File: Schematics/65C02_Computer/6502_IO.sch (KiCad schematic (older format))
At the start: 22 parts

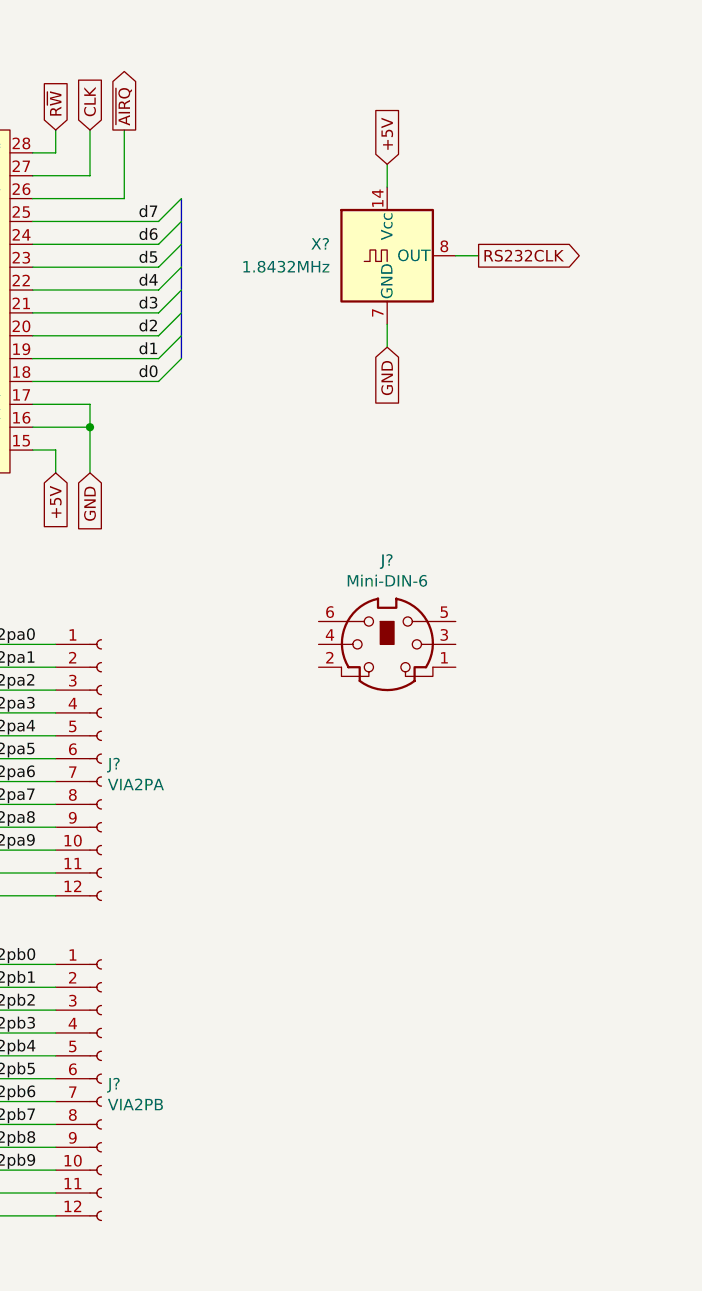
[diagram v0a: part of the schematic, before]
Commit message: Added keyboard microcontroller
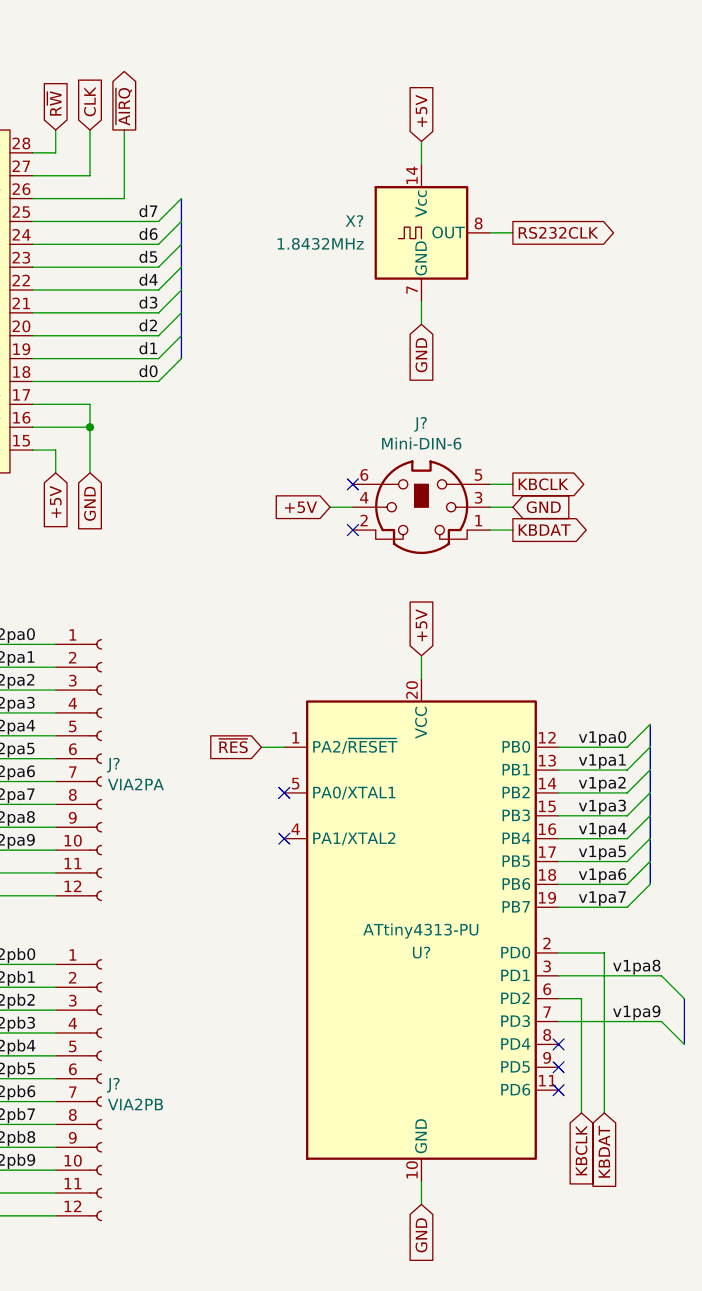
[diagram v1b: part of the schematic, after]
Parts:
- added U?: ATtiny4313-PU, Package_DIP:DIP-20_W7.62mm, symbol MCU_Microchip_ATtiny:ATtiny4313-PU
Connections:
- net +5V: now also J?.4, U?.20 (VCC)
- net GND: now also J?.3, U?.10 (GND)
- net v1pa0: now also U?.12 (PB0)
- net v1pa1: now also U?.13 (PB1)
- net v1pa2: now also U?.14 (PB2)
- net v1pa3: now also U?.15 (PB3)
- net v1pa4: now also U?.16 (PB4)
- net v1pa5: now also U?.17 (PB5)
- net v1pa6: now also U?.18 (PB6)
- net v1pa7: now also U?.19 (PB7)
- net v1pa8: now also U?.3 (PD1)
- net v1pa9: now also U?.7 (PD3)
- net ~RES: now also U?.1 (PA2/~RESET)
- net KBDAT: now reaches J?.1
- net KBDAT: now also U?.2 (PD0)
- net KBCLK: now reaches J?.5
- net KBCLK: now also U?.6 (PD2)
- no-connect marks 9 -> 16
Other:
- moved on the sheet: J?, X?
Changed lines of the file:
@@
 Wire Wire Line
 	5700 750  5700 1050
-Text GLabel 9400 1150 1    50   Input ~ 0
+Text GLabel 9550 1050 1    50   Input ~ 0
 +5V
-Text GLabel 9400 1950 3    50   Input ~ 0
+Text GLabel 9550 1850 3    50   Input ~ 0
 GND
 Wire Wire Line
-	9400 1950 9400 1850
-Wire Wire Line
-	9400 1150 9400 1250
-Text GLabel 9800 1550 2    50   Output ~ 0
+	9550 1850 9550 1750
+Wire Wire Line
+	9550 1050 9550 1150
+Text GLabel 9950 1450 2    50   Output ~ 0
 RS232CLK
 Wire Wire Line
-	9700 1550 9800 1550
+	9850 1450 9950 1450
 Wire Wire Line
 	2350 1950 2500 1950
@@
 L Connector:Mini-DIN-6 J?
 U 1 1 5F701D58
-P 9400 3250
-F 0 "J?" H 9400 3617 50  0000 C CNN
-F 1 "Mini-DIN-6" H 9400 3526 50  0000 C CNN
-F 2 "65C02_Computer:mini_din-6" H 9400 3250 50  0001 C CNN
-F 3 "http://service.powerdynamics.com/ec/Catalog17/Section%2011.pdf" H 9400 3250 50  0001 C CNN
-	1    9400 3250
+P 9550 2650
+F 0 "J?" H 9550 3017 50  0000 C CNN
+F 1 "Mini-DIN-6" H 9550 2926 50  0000 C CNN
+F 2 "65C02_Computer:mini_din-6" H 9550 2650 50  0001 C CNN
+F 3 "http://service.powerdynamics.com/ec/Catalog17/Section%2011.pdf" H 9550 2650 50  0001 C CNN
+	1    9550 2650
 	1    0    0    -1
 $EndComp
@@
 L Oscillator:ACO-xxxMHz X?
 U 1 1 5F4F8D3E
-P 9400 1550
+P 9550 1450
 AR Path="/5F4F8D3E" Ref="X?"  Part="1"
 AR Path="/5F14295C/5F4F8D3E" Ref="X?"  Part="1"
-F 0 "X?" H 9150 1600 50  0000 R CNN
-F 1 "1.8432MHz" H 9150 1500 50  0000 R CNN
-F 2 "Oscillator:Oscillator_DIP-14" H 9850 1200 50  0001 C CNN
-F 3 "http://www.conwin.com/datasheets/cx/cx030.pdf" H 9300 1550 50  0001 C CNN
-	1    9400 1550
+F 0 "X?" H 9300 1500 50  0000 R CNN
+F 1 "1.8432MHz" H 9300 1400 50  0000 R CNN
+F 2 "Oscillator:Oscillator_DIP-14" H 10000 1100 50  0001 C CNN
+F 3 "http://www.conwin.com/datasheets/cx/cx030.pdf" H 9450 1450 50  0001 C CNN
+	1    9550 1450
 	1    0    0    -1
 $EndComp
@@
 Entry Wire Line
 	7550 5450 7650 5550
+Text GLabel 9950 2550 2    50   Output ~ 0
+KBCLK
+Text GLabel 9950 2750 2    50   Output ~ 0
+KBDAT
+Text GLabel 9950 2650 2    50   Input ~ 0
+GND
+Text GLabel 9150 2650 0    50   Input ~ 0
++5V
+Wire Wire Line
+	9150 2650 9250 2650
+Wire Wire Line
+	9850 2650 9950 2650
+Wire Wire Line
+	9850 2550 9950 2550
+Wire Wire Line
+	9850 2750 9950 2750
+NoConn ~ 9250 2550
+NoConn ~ 9250 2750
+Text GLabel 9550 3300 1    50   Input ~ 0
++5V
+Text GLabel 9550 5700 3    50   Input ~ 0
+GND
+Text GLabel 8850 3700 0    50   Input ~ 0
+~RES
+Text Label 10450 3700 2    50   ~ 0
+v1pa0
+Text Label 10450 3800 2    50   ~ 0
+v1pa1
+Text Label 10450 3900 2    50   ~ 0
+v1pa2
+Text Label 10450 4000 2    50   ~ 0
+v1pa3
+Text Label 10450 4100 2    50   ~ 0
+v1pa4
+Text Label 10450 4200 2    50   ~ 0
+v1pa5
+Text Label 10450 4300 2    50   ~ 0
+v1pa6
+Text Label 10450 4400 2    50   ~ 0
+v1pa7
+Entry Wire Line
+	10450 3700 10550 3600
+Entry Wire Line
+	10450 3800 10550 3700
+Entry Wire Line
+	10450 3900 10550 3800
+Entry Wire Line
+	10450 4000 10550 3900
+Entry Wire Line
+	10450 4100 10550 4000
+Entry Wire Line
+	10450 4200 10550 4100
+Entry Wire Line
+	10450 4300 10550 4200
+Entry Wire Line
+	10450 4400 10550 4300
+Wire Wire Line
+	10150 3700 10450 3700
+Wire Wire Line
+	10150 3800 10450 3800
+Wire Wire Line
+	10150 3900 10450 3900
+Wire Wire Line
+	10150 4000 10450 4000
+Wire Wire Line
+	10150 4100 10450 4100
+Wire Wire Line
+	10150 4200 10450 4200
+Wire Wire Line
+	10150 4300 10450 4300
+Wire Wire Line
+	10150 4400 10450 4400
+Text GLabel 10350 5300 3    50   Input ~ 0
+KBDAT
+$Comp
+L MCU_Microchip_ATtiny:ATtiny4313-PU U?
+U 1 1 5E5D2E2B
+P 9550 4500
+F 0 "U?" H 9550 4400 50  0000 C CNN
+F 1 "ATtiny4313-PU" H 9550 4500 50  0000 C CNN
+F 2 "Package_DIP:DIP-20_W7.62mm" H 9550 4500 50  0001 C CIN
+F 3 "http://ww1.microchip.com/downloads/en/DeviceDoc/doc8246.pdf" H 9550 4500 50  0001 C CNN
+	1    9550 4500
+	1    0    0    -1
+$EndComp
+Wire Wire Line
+	8850 3700 8950 3700
+Wire Wire Line
+	10150 4800 10250 4800
+Text GLabel 10250 5300 3    50   Input ~ 0
+KBCLK
+NoConn ~ 8950 3900
+NoConn ~ 8950 4100
+Text Label 10600 4700 2    50   ~ 0
+v1pa8
+Text Label 10600 4900 2    50   ~ 0
+v1pa9
+Wire Wire Line
+	10250 5300 10250 4800
+Wire Wire Line
+	10350 5300 10350 4600
+Wire Wire Line
+	10150 4600 10350 4600
+Wire Wire Line
+	10150 4700 10600 4700
+Wire Wire Line
+	10150 4900 10600 4900
+Wire Wire Line
+	9550 5700 9550 5600
+Wire Wire Line
+	9550 3300 9550 3400
+Entry Wire Line
+	10600 4700 10700 4800
+Entry Wire Line
+	10600 4900 10700 5000
+Wire Bus Line
+	10700 5000 10700 4800
+NoConn ~ 10150 5000
+NoConn ~ 10150 5100
+NoConn ~ 10150 5200
 Wire Bus Line
 	5500 3000 5500 3400
@@
 	5950 3850 5950 4650
 Wire Bus Line
+	10550 3600 10550 4300
+Wire Bus Line
+	7550 4550 7550 5450
+Wire Bus Line
+	7550 3150 7550 4050
+Wire Bus Line
 	3450 4400 3450 5300
 Wire Bus Line
@@
 Wire Bus Line
 	1050 3000 1050 4100
-Wire Bus Line
-	7550 3150 7550 4050
-Wire Bus Line
-	7550 4550 7550 5450
 $EndSCHEMATC

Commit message: Various updates to schematic
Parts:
- added D4: BLINK, LED_THT:LED_D5.0mm_Clear, symbol Device:LED
- added R12: 270, Resistor_THT:R_Axial_DIN0207_L6.3mm_D2.5mm_P7.62mm_Horizontal, symbol Device:R
- C14, C15, C16: renamed from C?; footprint (none) -> Capacitor_THT:C_Disc_D3.4mm_W2.1mm_P2.50mm
- D1, D2, D3: renamed from D?; footprint (none) -> LED_THT:LED_D5.0mm_Clear
- J3: renamed from J?; footprint (none) -> Connector_USB:USB_Micro-B_Molex-105017-0001
- J4: renamed from J?; footprint (none) -> Connector_PinSocket_2.54mm:PinSocket_1x16_P2.54mm_Vertical
- J5, J6: renamed from J?; symbol Connector:Conn_01x12_Female -> Connector:Conn_01x12_Male
- R10, R11, R7, R8, R9: renamed from R?; footprint (none) -> Resistor_THT:R_Axial_DIN0207_L6.3mm_D2.5mm_P7.62mm_Horizontal
- RV1: renamed from RV?; footprint (none) -> Potentiometer_THT:Potentiometer_Runtron_RM-065_Vertical
- U12: renamed from U?; footprint Package_DIP:DIP-20_W7.62mm -> Package_DIP:DIP-20_W7.62mm_Socket
- gave numbers to parts that had none: 6
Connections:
- net +5V: now also R9.1; no longer D1.2 (A)
- net GND: now also D1.1 (K), D4.1 (K); no longer R9.1
- net v1pb0: now also R12.1
- net at R9.2: now also D1.2 (A); no longer D1.1 (K)
- new net: D4.2 (A), R12.2
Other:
- moved on the sheet: R9

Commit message: Small changes
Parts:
- U10: footprint Package_SO:SSOP-16_5.3x6.2mm_P0.65mm -> Package_SO:SSOP-16_4.4x5.2mm_P0.65mm
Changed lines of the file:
@@
 F 0 "U10" H 4650 2365 50  0000 C CNN
 F 1 "FT230XS" H 4650 2274 50  0000 C CNN
-F 2 "Package_SO:SSOP-16_5.3x6.2mm_P0.65mm" H 4650 2250 50  0001 C CNN
+F 2 "Package_SO:SSOP-16_4.4x5.2mm_P0.65mm" H 4650 2250 50  0001 C CNN
 F 3 "https://www.ftdichip.com/Support/Documents/DataSheets/ICs/DS_FT230X.pdf" H 4650 1750 50  0001 C CNN
 	1    4650 1750

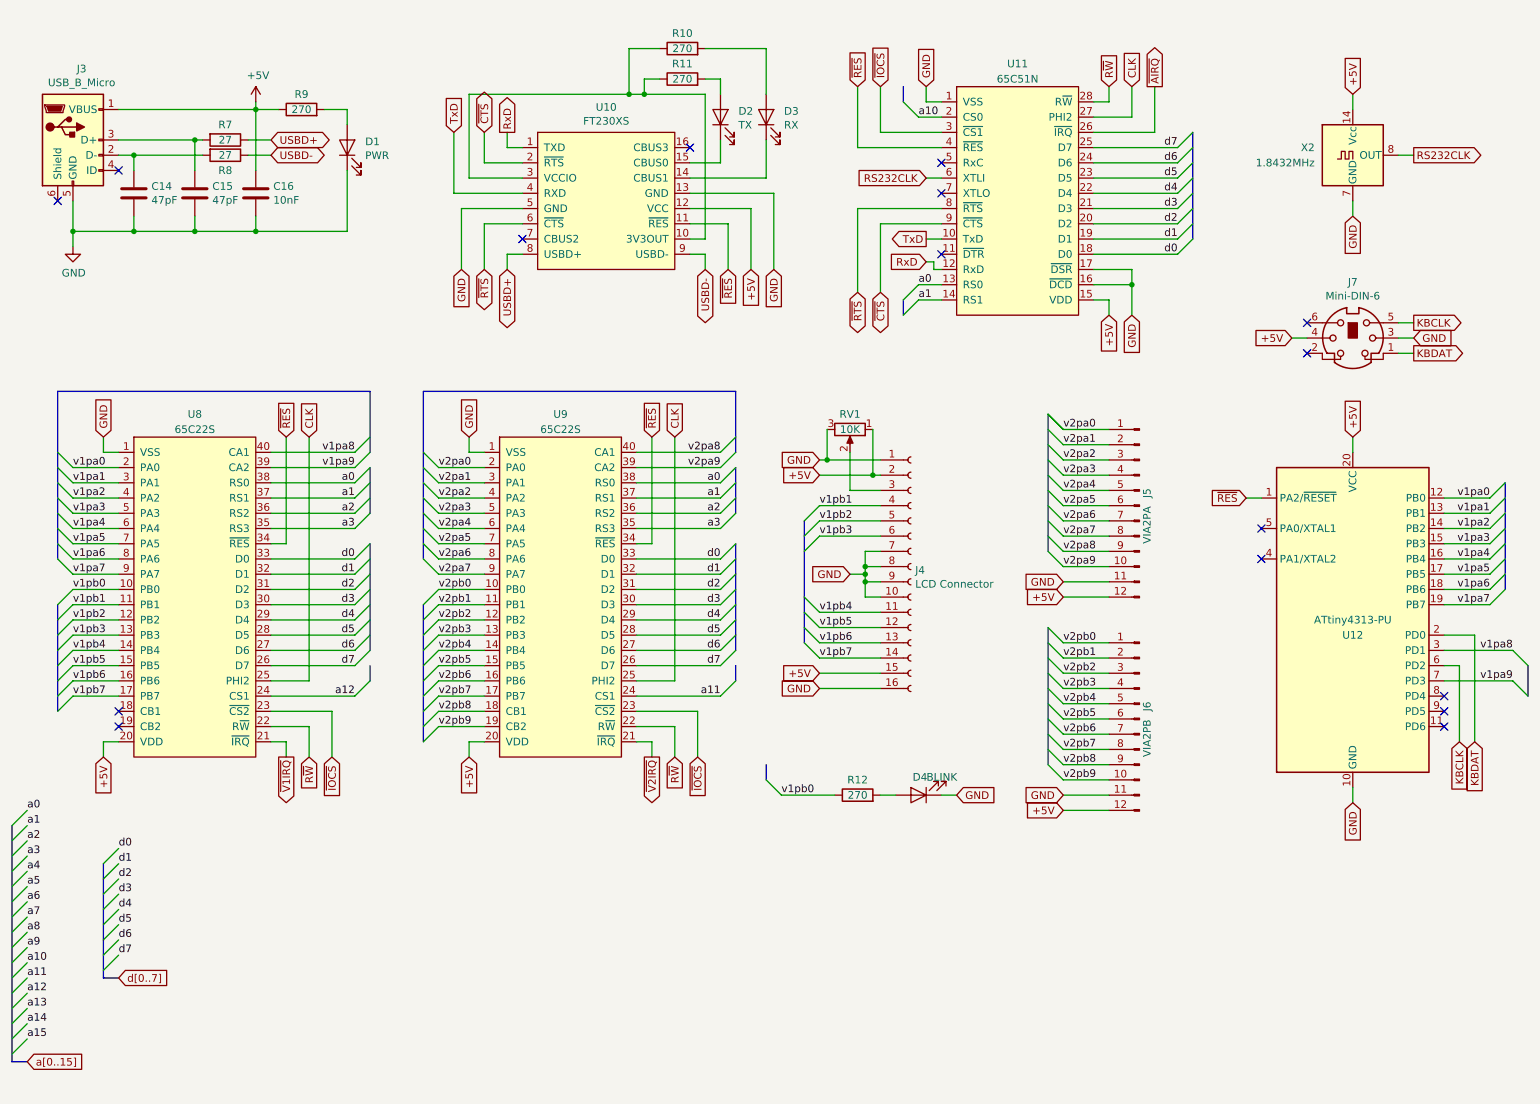
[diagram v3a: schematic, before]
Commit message: Reordered PCB components
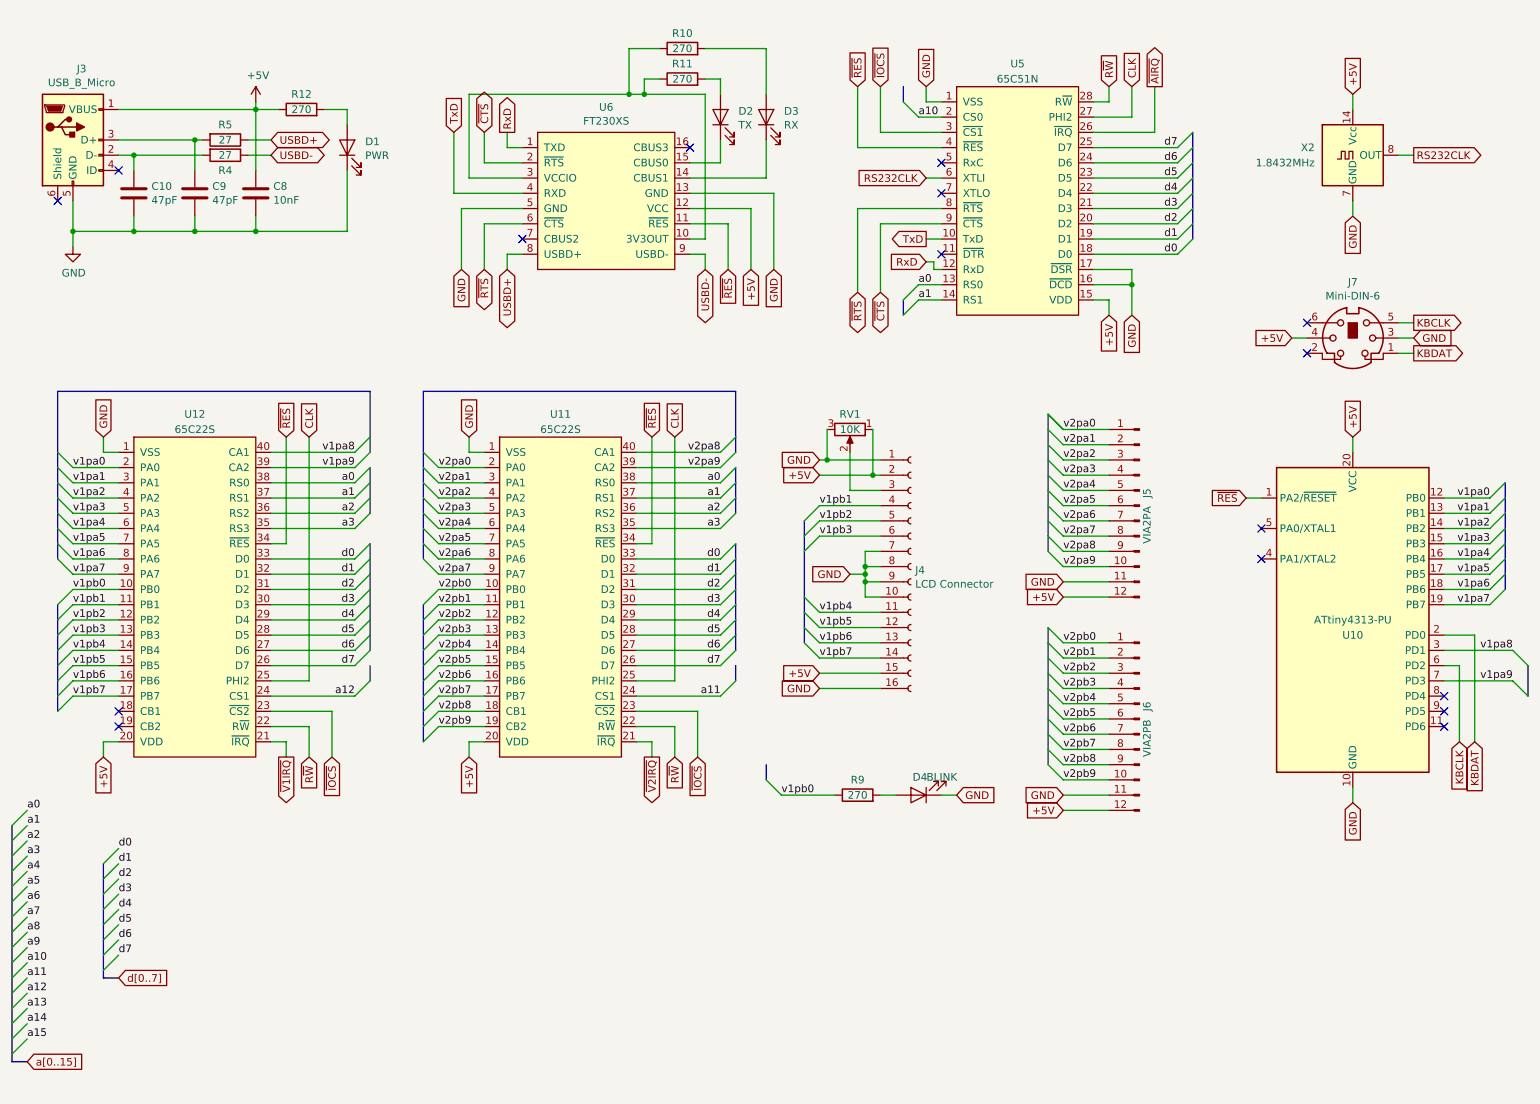
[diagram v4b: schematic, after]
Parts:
- renumbered C14 to C10, C16 to C8, C15 to C9, R9 to R12, R8 to R4, R7 to R5, R12 to R9, U12 to U10, U9 to U11, U8 to U12, U11 to U5, U10 to U6
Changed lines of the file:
@@
 $EndComp
 $Comp
-L Device:R R9
+L Device:R R12
 U 1 1 5F6AC848
 P 2650 1150
-F 0 "R9" V 2750 1150 50  0000 C CNN
+F 0 "R12" V 2750 1150 50  0000 C CNN
 F 1 "270" V 2650 1150 50  0000 C CNN
 F 2 "Resistor_THT:R_Axial_DIN0207_L6.3mm_D2.5mm_P7.62mm_Horizontal" V 2580 1150 50  0001 C CNN
@@
 P 1950 4300
 AR Path="/5F285E91" Ref="U?"  Part="1"
-AR Path="/5F14295C/5F285E91" Ref="U8"  Part="1"
-F 0 "U8" H 1950 5450 50  0000 C CNN
+AR Path="/5F14295C/5F285E91" Ref="U12"  Part="1"
+F 0 "U12" H 1950 5450 50  0000 C CNN
 F 1 "65C22S" H 1950 5350 50  0000 C CNN
 F 2 "Package_DIP:DIP-40_W15.24mm_Socket" H 2050 4300 50  0001 C CNN
@@
 P 4350 4300
 AR Path="/5F285E8B" Ref="U?"  Part="1"
-AR Path="/5F14295C/5F285E8B" Ref="U9"  Part="1"
-F 0 "U9" H 4350 5450 50  0000 C CNN
+AR Path="/5F14295C/5F285E8B" Ref="U11"  Part="1"
+F 0 "U11" H 4350 5450 50  0000 C CNN
 F 1 "65C22S" H 4350 5350 50  0000 C CNN
 F 2 "Package_DIP:DIP-40_W15.24mm_Socket" H 4450 4300 50  0001 C CNN
@@
 P 2350 1700
 AR Path="/5F26EF26" Ref="C?"  Part="1"
-AR Path="/5F14295C/5F26EF26" Ref="C16"  Part="1"
-F 0 "C16" H 2465 1746 50  0000 L CNN
+AR Path="/5F14295C/5F26EF26" Ref="C8"  Part="1"
+F 0 "C8" H 2465 1746 50  0000 L CNN
 F 1 "10nF" H 2465 1655 50  0000 L CNN
 F 2 "Capacitor_THT:C_Disc_D3.4mm_W2.1mm_P2.50mm" H 2388 1550 50  0001 C CNN
@@
 P 1950 1700
 AR Path="/5F26EF13" Ref="C?"  Part="1"
-AR Path="/5F14295C/5F26EF13" Ref="C15"  Part="1"
-F 0 "C15" H 2065 1746 50  0000 L CNN
+AR Path="/5F14295C/5F26EF13" Ref="C9"  Part="1"
+F 0 "C9" H 2065 1746 50  0000 L CNN
 F 1 "47pF" H 2065 1655 50  0000 L CNN
 F 2 "Capacitor_THT:C_Disc_D3.4mm_W2.1mm_P2.50mm" H 1988 1550 50  0001 C CNN
@@
 P 1550 1700
 AR Path="/5F26EF0D" Ref="C?"  Part="1"
-AR Path="/5F14295C/5F26EF0D" Ref="C14"  Part="1"
-F 0 "C14" H 1665 1746 50  0000 L CNN
+AR Path="/5F14295C/5F26EF0D" Ref="C10"  Part="1"
+F 0 "C10" H 1665 1746 50  0000 L CNN
 F 1 "47pF" H 1665 1655 50  0000 L CNN
 F 2 "Capacitor_THT:C_Disc_D3.4mm_W2.1mm_P2.50mm" H 1588 1550 50  0001 C CNN
@@
 P 2150 1450
 AR Path="/5F203CE6" Ref="R?"  Part="1"
-AR Path="/5F14295C/5F203CE6" Ref="R8"  Part="1"
-F 0 "R8" V 2250 1450 50  0000 C CNN
+AR Path="/5F14295C/5F203CE6" Ref="R4"  Part="1"
+F 0 "R4" V 2250 1450 50  0000 C CNN
 F 1 "27" V 2150 1450 50  0000 C CNN
 F 2 "Resistor_THT:R_Axial_DIN0207_L6.3mm_D2.5mm_P7.62mm_Horizontal" V 2080 1450 50  0001 C CNN
@@
 P 2150 1350
 AR Path="/5F203CE0" Ref="R?"  Part="1"
-AR Path="/5F14295C/5F203CE0" Ref="R7"  Part="1"
-F 0 "R7" V 2050 1350 50  0000 C CNN
+AR Path="/5F14295C/5F203CE0" Ref="R5"  Part="1"
+F 0 "R5" V 2050 1350 50  0000 C CNN
 F 1 "27" V 2150 1350 50  0000 C CNN
 F 2 "Resistor_THT:R_Axial_DIN0207_L6.3mm_D2.5mm_P7.62mm_Horizontal" V 2080 1350 50  0001 C CNN
@@
 P 4650 1750
 AR Path="/5F203CBA" Ref="U?"  Part="1"
-AR Path="/5F14295C/5F203CBA" Ref="U10"  Part="1"
-F 0 "U10" H 4650 2365 50  0000 C CNN
+AR Path="/5F14295C/5F203CBA" Ref="U6"  Part="1"
+F 0 "U6" H 4650 2365 50  0000 C CNN
 F 1 "FT230XS" H 4650 2274 50  0000 C CNN
 F 2 "Package_SO:SSOP-16_4.4x5.2mm_P0.65mm" H 4650 2250 50  0001 C CNN
@@
 P 7350 1750
 AR Path="/5F1AD73D" Ref="U?"  Part="1"
-AR Path="/5F14295C/5F1AD73D" Ref="U11"  Part="1"
-F 0 "U11" H 7350 2650 50  0000 C CNN
+AR Path="/5F14295C/5F1AD73D" Ref="U5"  Part="1"
+F 0 "U5" H 7350 2650 50  0000 C CNN
 F 1 "65C51N" H 7350 2550 50  0000 C CNN
 F 2 "Package_DIP:DIP-28_W15.24mm_Socket" H 7350 1750 50  0001 C CNN
@@
 KBDAT
 $Comp
-L MCU_Microchip_ATtiny:ATtiny4313-PU U12
+L MCU_Microchip_ATtiny:ATtiny4313-PU U10
 U 1 1 5E5D2E2B
 P 9550 4500
-F 0 "U12" H 9550 4400 50  0000 C CNN
+F 0 "U10" H 9550 4400 50  0000 C CNN
 F 1 "ATtiny4313-PU" H 9550 4500 50  0000 C CNN
 F 2 "Package_DIP:DIP-20_W7.62mm_Socket" H 9550 4500 50  0001 C CIN
@@
 GND
 $Comp
-L Device:R R12
+L Device:R R9
 U 1 1 5E7595AF
 P 6300 5650
-F 0 "R12" V 6400 5650 50  0000 C CNN
+F 0 "R9" V 6400 5650 50  0000 C CNN
 F 1 "270" V 6300 5650 50  0000 C CNN
 F 2 "Resistor_THT:R_Axial_DIN0207_L6.3mm_D2.5mm_P7.62mm_Horizontal" V 6230 5650 50  0001 C CNN
